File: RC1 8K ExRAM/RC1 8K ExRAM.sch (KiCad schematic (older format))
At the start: 29 parts, among them J1 Expansion, J2 ADDRESS, U1 74LS138, U2 74LS00, U3 74HC595, U4 74HC595, U5 HM62256BLP-7, U6 74LS244, U7 74LS244, U8 74LS245

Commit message: Routed D0-D7
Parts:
- D1, D2, D3: footprint (none) -> LEDs:LED_D5.0mm
- D4: footprint (none) -> Diodes_THT:D_DO-35_SOD27_P7.62mm_Horizontal
- J2: footprint (none) -> Pin_Headers:Pin_Header_Straight_2x09_Pitch2.54mm
- JP1: footprint (none) -> Pin_Headers:Pin_Header_Straight_1x02_Pitch2.54mm
- JP2: footprint (none) -> Pin_Headers:Pin_Header_Straight_1x03_Pitch2.54mm
- R1, R2, R3, R4: footprint (none) -> Resistors_THT:R_Axial_DIN0207_L6.3mm_D2.5mm_P10.16mm_Horizontal
- U2: footprint (none) -> Housings_DIP:DIP-14_W7.62mm_Socket
- U3, U4: footprint (none) -> Housings_DIP:DIP-16_W7.62mm_Socket
- U5: footprint DIP28 -> Housings_DIP:DIP-28_W15.24mm_Socket
- U6, U7, U8: footprint (none) -> Housings_DIP:DIP-20_W7.62mm_Socket
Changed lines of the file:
@@
 F 0 "J2" H 3475 2900 50  0000 C CNN
 F 1 "ADDRESS" H 3475 1900 50  0000 C CNN
-F 2 "" H 3425 2400 50  0001 C CNN
+F 2 "Pin_Headers:Pin_Header_Straight_2x09_Pitch2.54mm" H 3425 2400 50  0001 C CNN
 F 3 "" H 3425 2400 50  0001 C CNN
 	1    3425 2400
@@
 F 0 "U2" H 4550 2050 50  0000 C CNN
 F 1 "74LS00" H 4550 1900 50  0000 C CNN
-F 2 "" H 4550 2000 50  0001 C CNN
+F 2 "Housings_DIP:DIP-14_W7.62mm_Socket" H 4550 2000 50  0001 C CNN
 F 3 "" H 4550 2000 50  0001 C CNN
 	1    4550 2000
@@
 F 0 "U2" H 5900 1875 50  0000 C CNN
 F 1 "74LS00" H 5900 1725 50  0000 C CNN
-F 2 "" H 5900 1825 50  0001 C CNN
+F 2 "Housings_DIP:DIP-14_W7.62mm_Socket" H 5900 1825 50  0001 C CNN
 F 3 "" H 5900 1825 50  0001 C CNN
 	3    5900 1825
@@
 F 0 "U2" H 5900 1375 50  0000 C CNN
 F 1 "74LS00" H 5900 1225 50  0000 C CNN
-F 2 "" H 5900 1325 50  0001 C CNN
+F 2 "Housings_DIP:DIP-14_W7.62mm_Socket" H 5900 1325 50  0001 C CNN
 F 3 "" H 5900 1325 50  0001 C CNN
 	2    5900 1325
@@
 F 0 "U2" H 8950 10175 50  0000 C CNN
 F 1 "74LS00" H 8950 10025 50  0000 C CNN
-F 2 "" H 8950 10125 50  0001 C CNN
+F 2 "Housings_DIP:DIP-14_W7.62mm_Socket" H 8950 10125 50  0001 C CNN
 F 3 "" H 8950 10125 50  0001 C CNN
 	4    8950 10125
@@
 F 0 "U5" H 11700 4150 50  0000 C CNN
 F 1 "HM62256BLP-7" V 11700 3425 50  0000 C CNN
-F 2 "DIP28" H 11700 3425 50  0001 C CIN
+F 2 "Housings_DIP:DIP-28_W15.24mm_Socket" H 11700 3425 50  0001 C CIN
 F 3 "" H 11700 3425 50  0001 C CNN
 	1    11700 3425
@@
 F 0 "U8" H 11700 7800 50  0000 C BNN
 F 1 "74LS245" H 11700 7550 50  0000 C TNN
-F 2 "" H 11700 7675 50  0001 C CNN
+F 2 "Housings_DIP:DIP-20_W7.62mm_Socket" H 11700 7675 50  0001 C CNN
 F 3 "" H 11700 7675 50  0001 C CNN
 	1    11700 7675
@@
 F 0 "U7" H 11700 6600 50  0000 C CNN
 F 1 "74LS244" H 11700 6300 50  0000 C CNN
-F 2 "" H 11700 6450 50  0001 C CNN
+F 2 "Housings_DIP:DIP-20_W7.62mm_Socket" H 11700 6450 50  0001 C CNN
 F 3 "" H 11700 6450 50  0001 C CNN
 	1    11700 6450
@@
 F 0 "U6" H 11700 5375 50  0000 C CNN
 F 1 "74LS244" H 11700 5075 50  0000 C CNN
-F 2 "" H 11700 5225 50  0001 C CNN
+F 2 "Housings_DIP:DIP-20_W7.62mm_Socket" H 11700 5225 50  0001 C CNN
 F 3 "" H 11700 5225 50  0001 C CNN
 	1    11700 5225
@@
 F 0 "U3" H 7500 7275 50  0000 C CNN
 F 1 "74HC595" V 7500 6675 50  0000 C CNN
-F 2 "" H 7500 6675 50  0001 C CNN
+F 2 "Housings_DIP:DIP-16_W7.62mm_Socket" H 7500 6675 50  0001 C CNN
 F 3 "" H 7500 6675 50  0001 C CNN
 	1    7500 6675
@@
 F 0 "U4" H 7500 8575 50  0000 C CNN
 F 1 "74HC595" V 7500 7975 50  0000 C CNN
-F 2 "" H 7500 7975 50  0001 C CNN
+F 2 "Housings_DIP:DIP-16_W7.62mm_Socket" H 7500 7975 50  0001 C CNN
 F 3 "" H 7500 7975 50  0001 C CNN
 	1    7500 7975
@@
 F 0 "JP1" H 7000 2880 50  0000 C CNN
 F 1 "USB_PWR" H 7010 2740 50  0000 C CNN
-F 2 "" H 7000 2800 50  0001 C CNN
+F 2 "Pin_Headers:Pin_Header_Straight_1x02_Pitch2.54mm" H 7000 2800 50  0001 C CNN
 F 3 "" H 7000 2800 50  0001 C CNN
 	1    7000 2800
@@
 F 0 "R1" V 5905 3800 50  0000 C CNN
 F 1 "220" V 5825 3800 50  0000 C CNN
-F 2 "" V 5755 3800 50  0001 C CNN
+F 2 "Resistors_THT:R_Axial_DIN0207_L6.3mm_D2.5mm_P10.16mm_Horizontal" V 5755 3800 50  0001 C CNN
 F 3 "" H 5825 3800 50  0001 C CNN
 	1    5825 3800
@@
 F 0 "D1" H 6100 3925 50  0000 L CNN
 F 1 "BUSY" H 6150 3725 50  0000 C CNN
-F 2 "" V 6150 3800 50  0001 C CNN
+F 2 "LEDs:LED_D5.0mm" V 6150 3800 50  0001 C CNN
 F 3 "" V 6150 3800 50  0001 C CNN
 	1    6150 3800
@@
 F 0 "D2" H 6100 4200 50  0000 L CNN
 F 1 "DATA" H 6150 4000 50  0000 C CNN
-F 2 "" V 6150 4075 50  0001 C CNN
+F 2 "LEDs:LED_D5.0mm" V 6150 4075 50  0001 C CNN
 F 3 "" V 6150 4075 50  0001 C CNN
 	1    6150 4075
@@
 F 0 "D3" H 6100 4475 50  0000 L CNN
 F 1 "CLK" H 6150 4275 50  0000 C CNN
-F 2 "" V 6150 4350 50  0001 C CNN
+F 2 "LEDs:LED_D5.0mm" V 6150 4350 50  0001 C CNN
 F 3 "" V 6150 4350 50  0001 C CNN
 	1    6150 4350
@@
 F 0 "R2" V 5905 4075 50  0000 C CNN
 F 1 "220" V 5825 4075 50  0000 C CNN
-F 2 "" V 5755 4075 50  0001 C CNN
+F 2 "Resistors_THT:R_Axial_DIN0207_L6.3mm_D2.5mm_P10.16mm_Horizontal" V 5755 4075 50  0001 C CNN
 F 3 "" H 5825 4075 50  0001 C CNN
 	1    5825 4075
@@
 F 0 "R3" V 5905 4350 50  0000 C CNN
 F 1 "220" V 5825 4350 50  0000 C CNN
-F 2 "" V 5755 4350 50  0001 C CNN
+F 2 "Resistors_THT:R_Axial_DIN0207_L6.3mm_D2.5mm_P10.16mm_Horizontal" V 5755 4350 50  0001 C CNN
 F 3 "" H 5825 4350 50  0001 C CNN
 	1    5825 4350
@@
 F 0 "R4" V 5155 1100 50  0000 C CNN
 F 1 "10k" V 5075 1100 50  0000 C CNN
-F 2 "" V 5005 1100 50  0001 C CNN
+F 2 "Resistors_THT:R_Axial_DIN0207_L6.3mm_D2.5mm_P10.16mm_Horizontal" V 5005 1100 50  0001 C CNN
 F 3 "" H 5075 1100 50  0001 C CNN
 	1    5075 1100
@@
 F 0 "D4" H 6950 3155 50  0000 L CNN
 F 1 "1n914" H 6850 2995 50  0000 L CNN
-F 2 "" V 7000 3075 50  0001 C CNN
+F 2 "Diodes_THT:D_DO-35_SOD27_P7.62mm_Horizontal" V 7000 3075 50  0001 C CNN
 F 3 "" V 7000 3075 50  0001 C CNN
 	1    7000 3075
@@
 F 0 "JP2" H 9975 6275 50  0000 L CNN
 F 1 "ReadOnly" H 9925 6475 50  0000 C BNN
-F 2 "" H 9925 6375 50  0001 C CNN
+F 2 "Pin_Headers:Pin_Header_Straight_1x03_Pitch2.54mm" H 9925 6375 50  0001 C CNN
 F 3 "" H 9925 6375 50  0001 C CNN
 	1    9925 6375

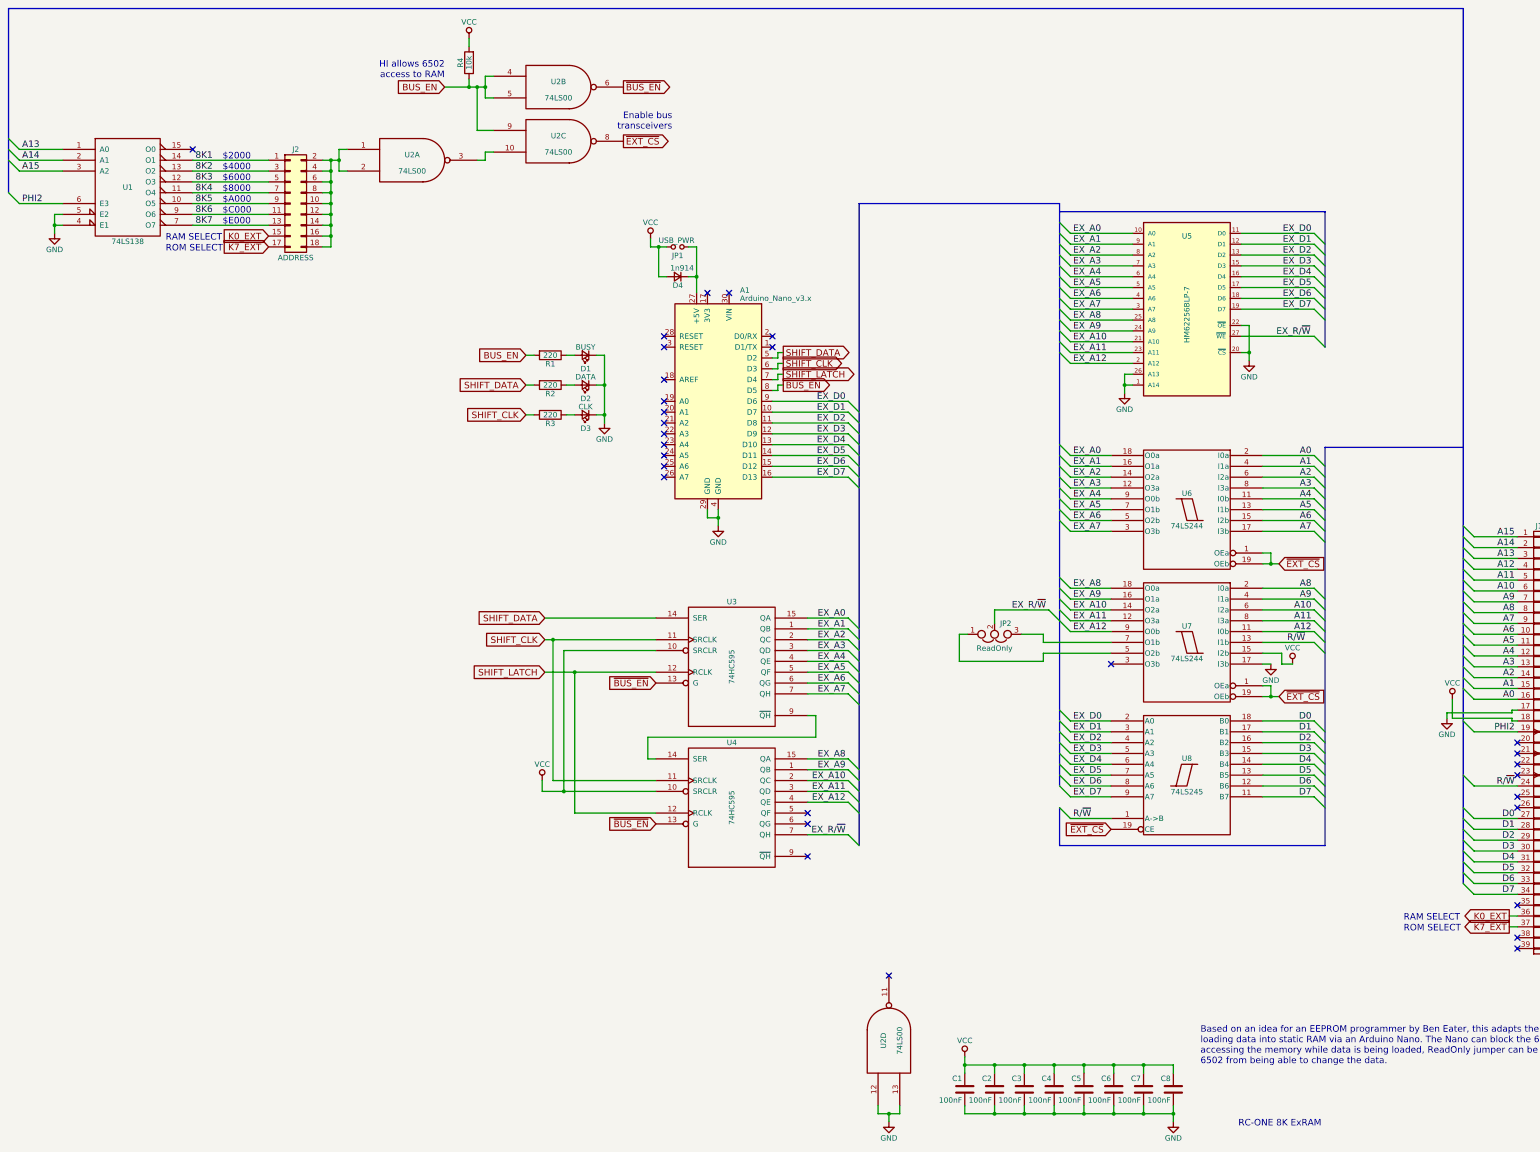
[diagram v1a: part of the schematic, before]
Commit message: 8K ExRAM layout and silkscreen done
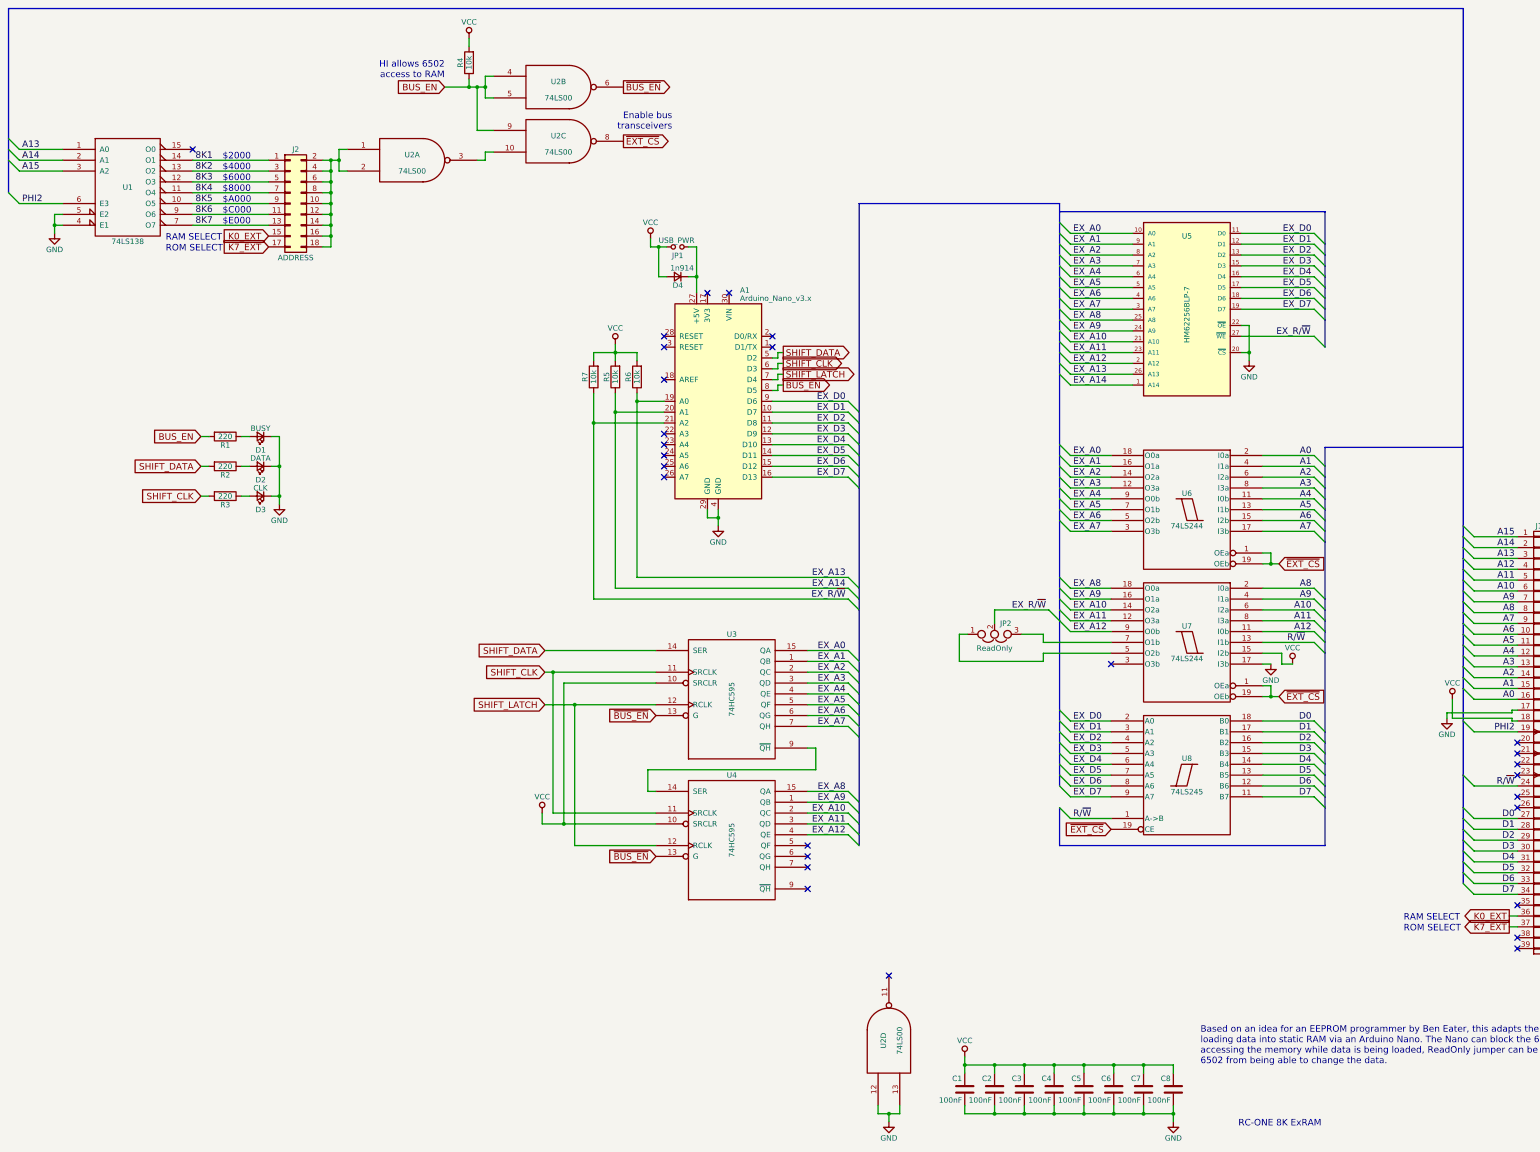
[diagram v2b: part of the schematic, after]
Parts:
- added R5, R6, R7: 10k, Resistors_THT:R_Axial_DIN0207_L6.3mm_D2.5mm_P10.16mm_Horizontal, symbol R
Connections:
- net EX_R/~W: now also A1.21 (A2), R7.1; no longer U4.7 (QH)
- net GND: no longer U5.1 (A14), U5.26 (A13)
- net VCC: now also R5.2, R6.2, R7.2
- net EX_A13: now reaches A1.19 (A0)
- net EX_A13: now also U5.26 (A13), R6.1
- net EX_A14: now reaches A1.20 (A1)
- net EX_A14: now also U5.1 (A14), R5.1
- no-connect marks 30 -> 28
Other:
- moved on the sheet: D1, D2, D3, R1, R2, R3, U3, U4

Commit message: Gerber export
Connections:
- net RESET: now reaches J1.20 (RESET)
- net RESET: now also A1.26 (A7)
- no-connect marks 28 -> 26

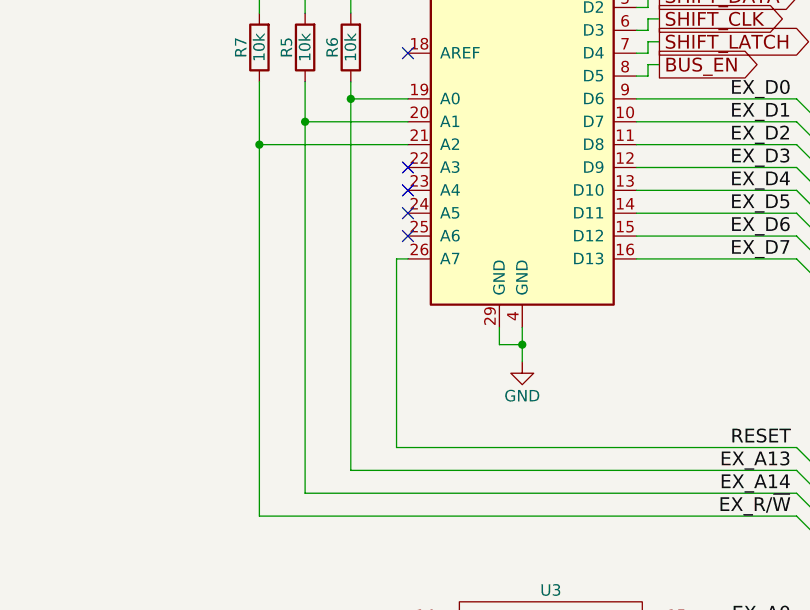
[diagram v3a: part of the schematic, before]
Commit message: A7 not usable as digital pin on Nano (appearantly)
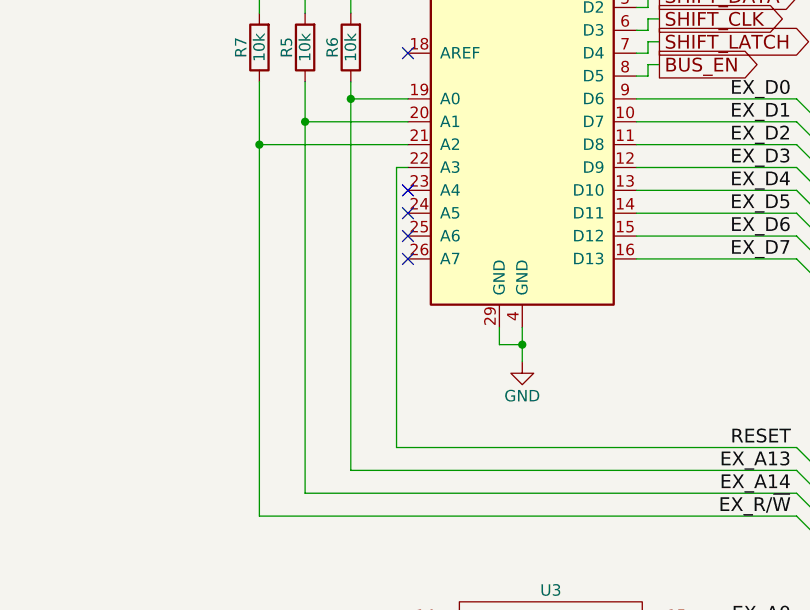
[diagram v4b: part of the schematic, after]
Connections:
- net RESET: now also A1.22 (A3); no longer A1.26 (A7)
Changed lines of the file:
@@
 $EndComp
 NoConn ~ 6875 4025
-NoConn ~ 6875 4525
 NoConn ~ 6875 4625
 NoConn ~ 6875 4725
@@
 	8575 5750 8675 5850
 Wire Wire Line
-	6875 4925 6825 4925
-Wire Wire Line
-	6825 4925 6825 5750
+	6825 4525 6825 5750
 Wire Wire Line
 	6825 5750 8575 5750
+Wire Wire Line
+	6825 4525 6875 4525
+NoConn ~ 6875 4925
 $EndSCHEMATC
